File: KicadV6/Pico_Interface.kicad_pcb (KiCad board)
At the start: 2 copper layers, 55 x 101.1 mm, 6 parts, among them J0 Conn_02x06_Odd_Even, J1 Conn_02x06_Odd_Even, J2 Conn_02x06_Odd_Even, J3 Conn_02x06_Odd_Even, J4 Conn_01x03_Male, U1 Pico

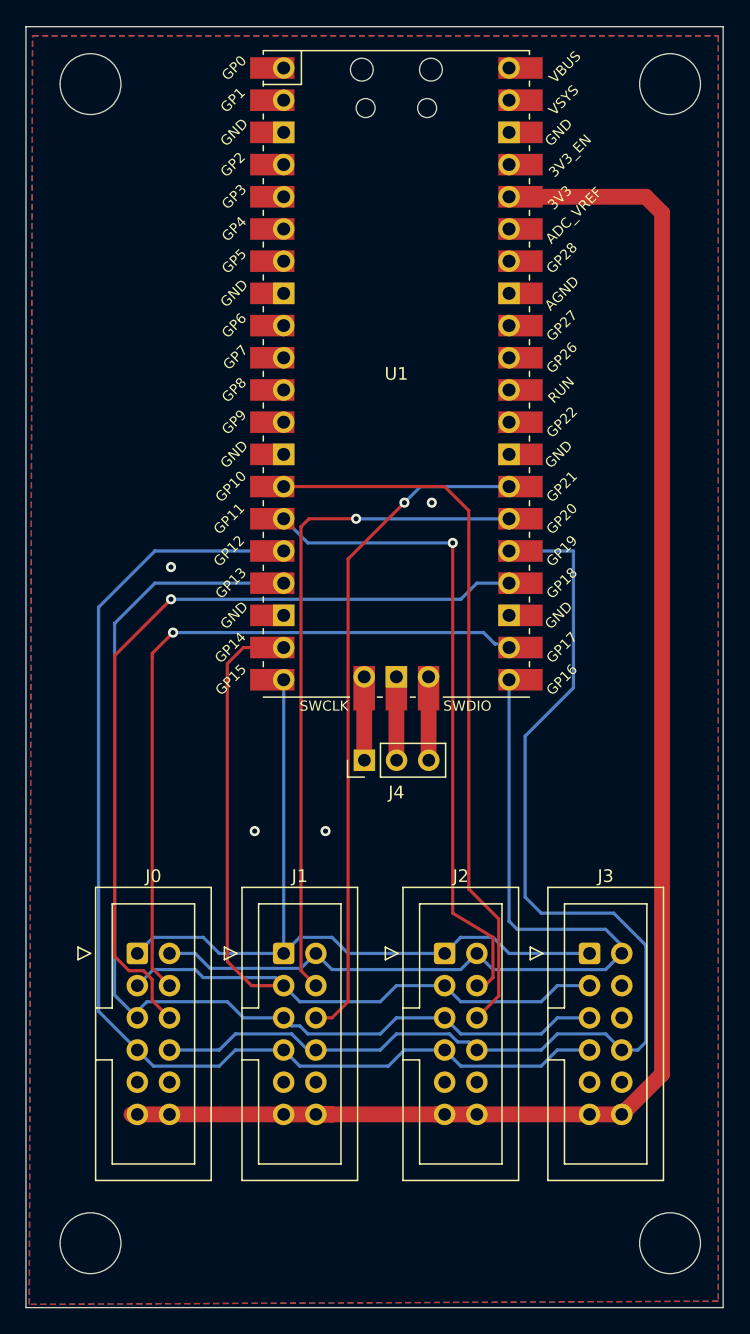
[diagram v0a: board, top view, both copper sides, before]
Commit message: Started change of layout
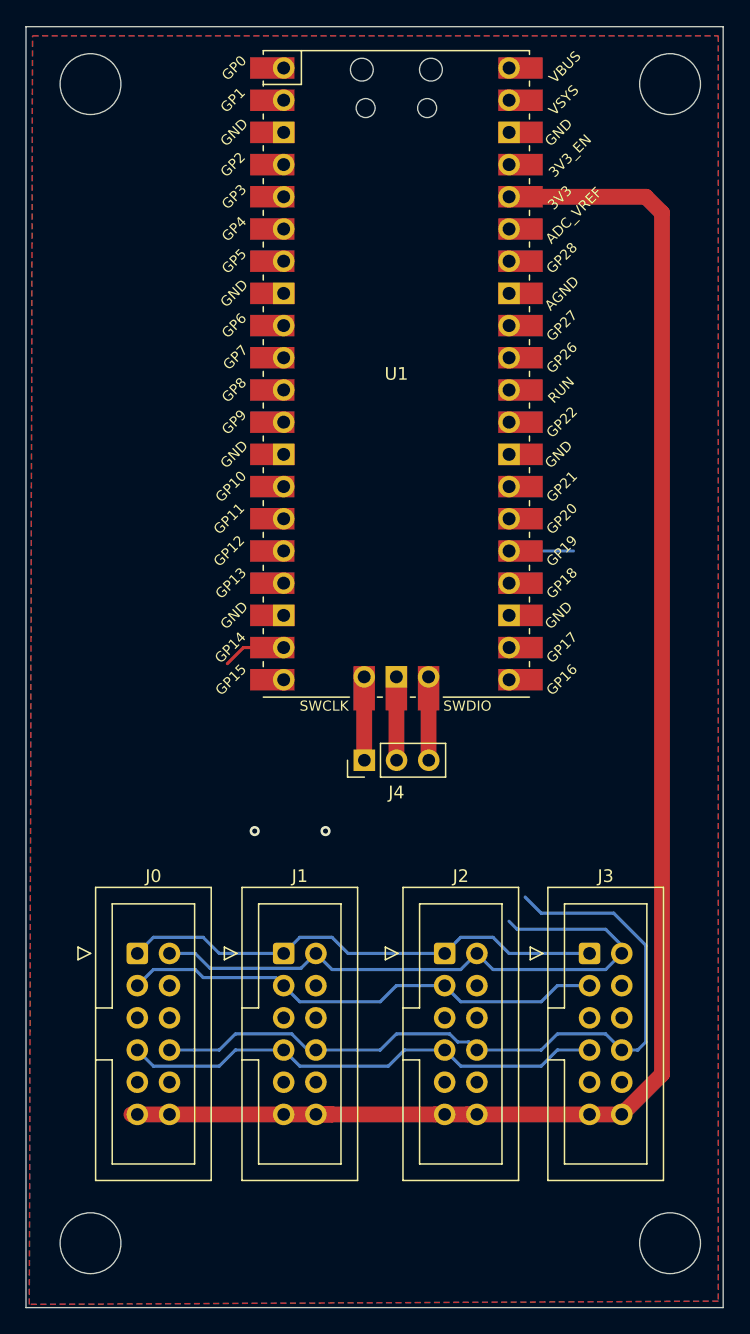
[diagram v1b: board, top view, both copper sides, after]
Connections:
- J0 pad 1: /DVDD_EN -> /DVDD_EN_0
- J0 pad 2: /AVDD_EN -> /AVDD_EN_0
- J0 pad 5: /MCLK_I -> GND
- J1 pad 1: /DVDD_EN -> /DVDD_EN_1
- J1 pad 2: /AVDD_EN -> /AVDD_EN_1
- J1 pad 5: /MCLK_I -> GND
- J2 pad 1: /DVDD_EN -> /DVDD_EN_2
- J2 pad 2: /AVDD_EN -> /AVDD_EN_2
- J2 pad 5: /MCLK_I -> GND
- J3 pad 1: /DVDD_EN -> /DVDD_EN_3
- J3 pad 2: /AVDD_EN -> /AVDD_EN_3
- J3 pad 5: /MCLK_I -> GND
- U1 pad 10: unconnected-(U1-Pad10) -> /DCTRL_O_1
- U1 pad 11: unconnected-(U1-Pad11) -> /DCTRL_O_2
- U1 pad 12: unconnected-(U1-Pad12) -> /DCTRL_O_3
- U1 pad 14: /DCTRL_I_2 -> /DCTRL_I_0
- U1 pad 15: /DCTRL_O_2 -> /DCTRL_I_1
- U1 pad 16: /MCLK_OE -> /DCTRL_I_2
- U1 pad 17: /MCLK_I -> /DCTRL_I_3
- U1 pad 19: /MCLK_O -> /DCTRL_OE
- U1 pad 20: /DVDD_EN -> unconnected-(U1-Pad20)
- U1 pad 21: /AVDD_EN -> /MCLK_O
- U1 pad 22: /DCTRL_O_0 -> /MCLK_OE
- U1 pad 24: /DCTRL_I_0 -> /AVDD_EN_3
- U1 pad 25: /DCTRL_OE -> /AVDD_EN_2
- U1 pad 26: /DCTRL_O_1 -> /AVDD_EN_1
- U1 pad 27: /DCTRL_I_1 -> /AVDD_EN_0
- U1 pad 9: unconnected-(U1-Pad9) -> /DCTRL_O_0
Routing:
- net /MCLK_I: track 85.6 -> 0.00 mm
- net /AVDD_EN: track 68.1 -> 0.00 mm
- net /DCTRL_I_0: track 64.5 -> 0.00 mm, vias 1 -> 0
- net /DVDD_EN: track 60.4 -> 0.00 mm
- net /DCTRL_I_2: track 57.1 -> 0.00 mm
- net /DCTRL_O_0: track 56.1 -> 0.00 mm, vias 1 -> 0
- net /DCTRL_O_1: track 53.4 -> 0.00 mm, vias 1 -> 0
- net /DCTRL_I_1: track 53.1 -> 0.00 mm, vias 1 -> 0
- net /MCLK_OE: track 91.5 -> 39.2 mm
- net /DCTRL_O_2: track 51.7 -> 0.64 mm, vias 1 -> 0
- net /DVDD_EN_1: track 0.00 -> 38.8 mm
- net /DCTRL_OE: track 93.7 -> 64.7 mm
- net /MCLK_O: track 72.5 -> 87.9 mm
- net /AVDD_EN_2: track 0.00 -> 5.08 mm
- net GND: track 6.59 -> 7.10 mm, vias 4 -> 2

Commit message: Added Trigger/Bussy and 3.3V LDO
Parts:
- added C1: 10uF, Capacitor_SMD:C_1206_3216Metric_Pad1.33x1.80mm_HandSolder, F.Cu at (129.0, 65.8)
- added J5: Conn_01x02_Male, Connector_PinHeader_2.54mm:PinHeader_1x02_P2.54mm_Vertical, F.Cu at (123.2, 58.4)
- added J6: Conn_01x03_Male, Connector_PinHeader_2.54mm:PinHeader_1x03_P2.54mm_Vertical, F.Cu at (83.2, 55.0)
- added J7: Conn_01x02_Male, Connector_PinHeader_2.54mm:PinHeader_1x02_P2.54mm_Vertical, F.Cu at (123.2, 48.3)
- added U2: NCP1117-3.3_SOT223, Package_TO_SOT_SMD:SOT-223-3_TabPin2, F.Cu at (129.5, 59.1)
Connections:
- U1 pad 1: unconnected-(U1-Pad1) -> /TRIGGER
- U1 pad 13: unconnected-(U1-Pad13) -> GND
- U1 pad 2: unconnected-(U1-Pad2) -> /BUSY
- U1 pad 28: unconnected-(U1-Pad28) -> GND
- U1 pad 3: unconnected-(U1-Pad3) -> GND
- U1 pad 36: +3.3V -> +3.3VP
- U1 pad 38: unconnected-(U1-Pad38) -> GND
- U1 pad 4: unconnected-(U1-Pad4) -> /DVDD_EN_0
- U1 pad 40: unconnected-(U1-Pad40) -> +5VP
- U1 pad 5: unconnected-(U1-Pad5) -> /DVDD_EN_1
- U1 pad 6: unconnected-(U1-Pad6) -> /DVDD_EN_2
- U1 pad 7: unconnected-(U1-Pad7) -> /DVDD_EN_3
- U1 pad 8: unconnected-(U1-Pad8) -> GND
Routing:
- net /MCLK_O: track 87.9 -> 38.8 mm
- net /DVDD_EN_1: track 38.8 -> 0.00 mm
- net /DCTRL_OE: track 64.7 -> 38.8 mm
- net +3.3V: track 124.8 -> 137.5 mm
- net +5V: track 0.00 -> 8.57 mm
- net /AVDD_EN_2: track 5.08 -> 0.00 mm
- net +5VP: track 0.00 -> 5.08 mm
- net +3.3VP: track 0.00 -> 5.08 mm
- net /DCTRL_O_2: track 0.64 -> 0.00 mm
- net GND: track 7.10 -> 6.59 mm, vias 2 -> 0
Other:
- board text added: "Busy"
- board text added: "GND"
- board text added: "Trigger"

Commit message: Kicad PCB Routed and ready for Production
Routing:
- net /DVDD_EN_3: track 0.00 -> 84.8 mm
- net /DCTRL_O_2: track 0.00 -> 81.2 mm, vias 0 -> 2
- net /DVDD_EN_1: track 0.00 -> 79.1 mm
- net /DVDD_EN_0: track 0.00 -> 74.2 mm
- net /DCTRL_O_3: track 0.00 -> 72.4 mm, vias 0 -> 1
- net /DVDD_EN_2: track 0.00 -> 69.0 mm
- net /DCTRL_O_1: track 0.00 -> 65.6 mm
- net /AVDD_EN_0: track 0.00 -> 64.6 mm, vias 0 -> 1
- net /DCTRL_O_0: track 0.00 -> 63.8 mm
- net /DCTRL_I_3: track 0.00 -> 61.3 mm
- net /DCTRL_I_2: track 0.00 -> 60.9 mm
- net /DCTRL_OE: track 38.8 -> 95.8 mm, vias 0 -> 1
- net /DCTRL_I_0: track 0.00 -> 54.3 mm, vias 0 -> 1
- net /AVDD_EN_1: track 0.00 -> 44.8 mm, vias 0 -> 1
- net /DCTRL_I_1: track 0.00 -> 42.9 mm
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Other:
- board text added: "Pico Readout for ITS Outer Barrel Model"
- board text added: "V1.0 Oct 2022 RUL"

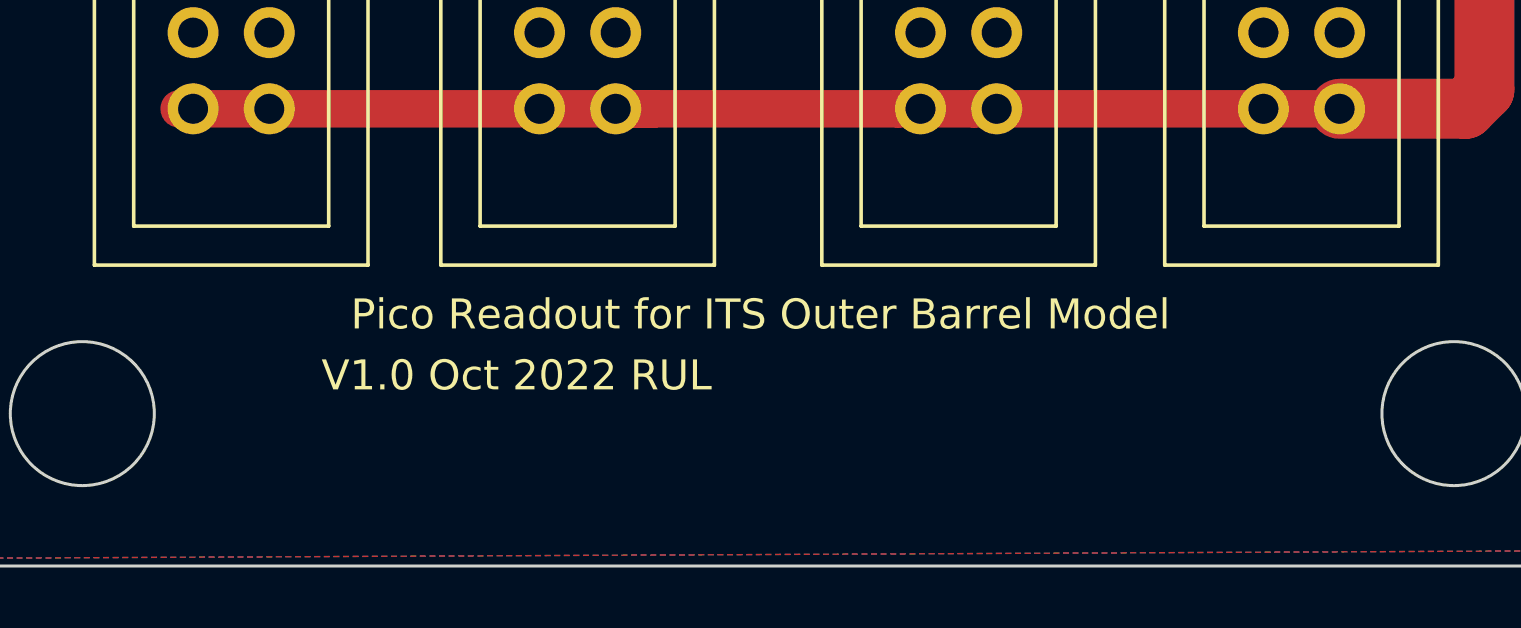
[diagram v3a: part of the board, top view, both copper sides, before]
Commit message: Fix Silk text
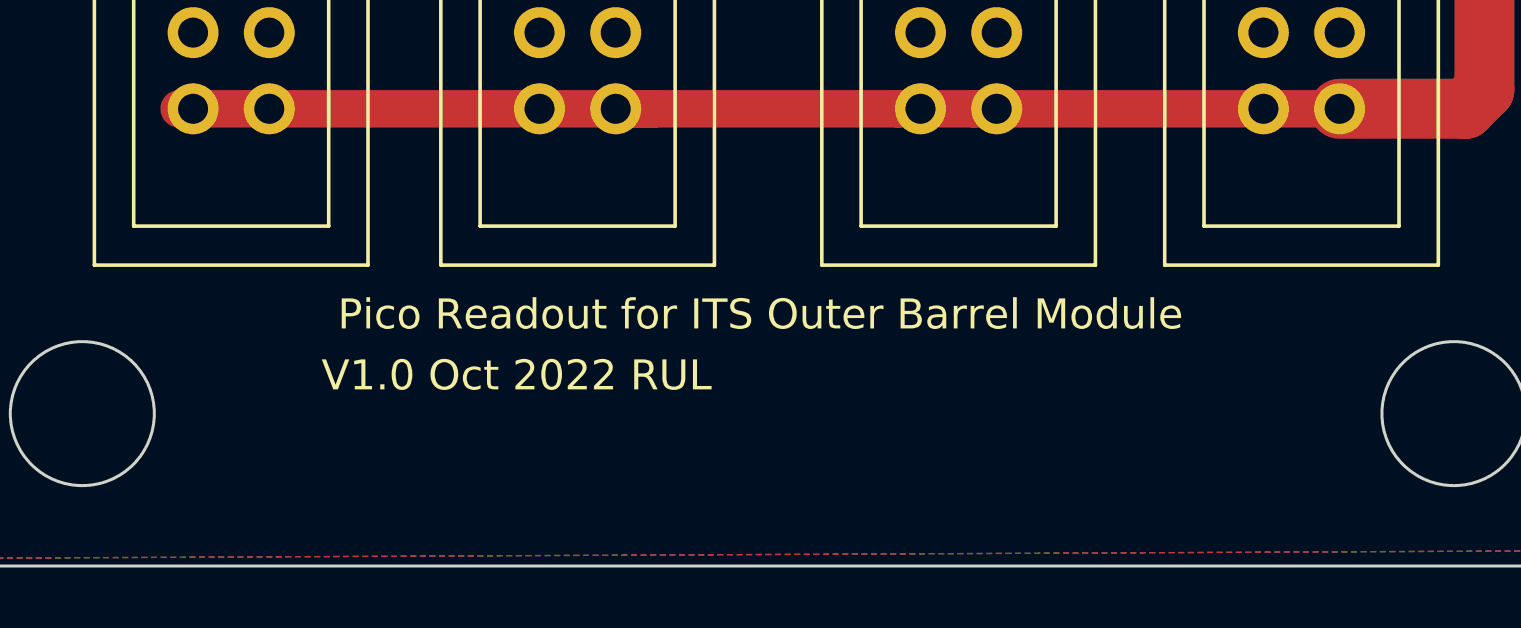
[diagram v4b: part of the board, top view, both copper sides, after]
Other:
- board text added: "Pico Readout for ITS Outer Barrel Module"
- board text removed: "Pico Readout for ITS Outer Barrel Model"
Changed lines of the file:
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@@
     (effects (font (size 1 1) (thickness 0.15)))
   )
-  (gr_text "Pico Readout for ITS Outer Barrel Model" (at 107.696 137.668) (layer "F.SilkS")
+  (gr_text "Pico Readout for ITS Outer Barrel Module" (at 107.696 137.668) (layer "F.SilkS")
     (effects (font (size 1 1) (thickness 0.15)))
   )
